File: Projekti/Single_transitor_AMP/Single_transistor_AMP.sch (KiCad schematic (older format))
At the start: 10 parts, among them P1 CONN_01X02, P2 CONN_01X02, Q1 BC549

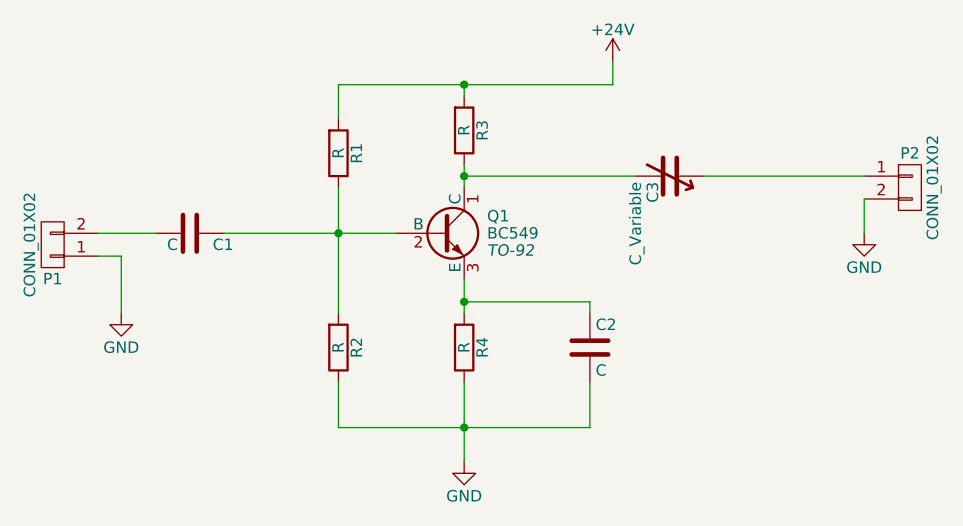
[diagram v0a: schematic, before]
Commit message: Single transitor amp
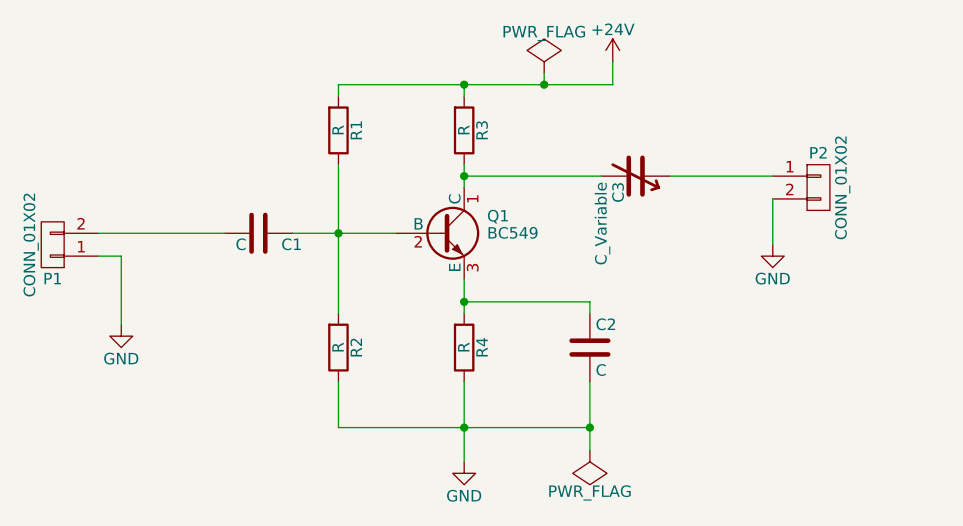
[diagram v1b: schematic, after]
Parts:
- Q1: footprint TO-92 -> TO_SOT_Packages_THT:TO-92_Inline_Wide
- R1, R2, R3, R4: footprint (none) -> Resistors_THT:R_Axial_DIN0309_L9.0mm_D3.2mm_P15.24mm_Horizontal
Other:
- moved on the sheet: C1, C3, P2, R1
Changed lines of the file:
@@
 encoding utf-8
 Sheet 1 1
-Title ""
-Date ""
-Rev ""
-Comp ""
+Title "Single transitor (BC549) amplifier"
+Date "2017-03-23"
+Rev "1.0"
+Comp "VeA"
 Comment1 ""
 Comment2 ""
@@
 F 0 "Q1" H 5800 4025 50  0000 L CNN
 F 1 "BC549" H 5800 3950 50  0000 L CNN
-F 2 "TO-92" H 5800 3875 50  0000 L CIN
-F 3 "" H 5600 3950 50  0000 L CNN
+F 2 "TO_SOT_Packages_THT:TO-92_Inline_Wide" H 5800 3875 50  0001 L CIN
+F 3 "http://pdf1.alldatasheet.com/datasheet-pdf/view/273461/DCCOM/BC549.html" H 5600 3950 50  0001 L CNN
 	1    5600 3950
 	1    0    0    -1
@@
 L R R1
 U 1 1 58D39335
-P 5150 3600
-F 0 "R1" V 5230 3600 50  0000 C CNN
-F 1 "R" V 5150 3600 50  0000 C CNN
-F 2 "" V 5080 3600 50  0000 C CNN
-F 3 "" H 5150 3600 50  0000 C CNN
-	1    5150 3600
+P 5150 3500
+F 0 "R1" V 5230 3500 50  0000 C CNN
+F 1 "R" V 5150 3500 50  0000 C CNN
+F 2 "Resistors_THT:R_Axial_DIN0309_L9.0mm_D3.2mm_P15.24mm_Horizontal" V 5080 3500 50  0001 C CNN
+F 3 "" H 5150 3500 50  0000 C CNN
+	1    5150 3500
 	1    0    0    1
 $EndComp
@@
 F 0 "R2" V 5230 4450 50  0000 C CNN
 F 1 "R" V 5150 4450 50  0000 C CNN
-F 2 "" V 5080 4450 50  0000 C CNN
+F 2 "Resistors_THT:R_Axial_DIN0309_L9.0mm_D3.2mm_P15.24mm_Horizontal" V 5080 4450 50  0001 C CNN
 F 3 "" H 5150 4450 50  0000 C CNN
 	1    5150 4450
@@
 $EndComp
 Wire Wire Line
-	4650 3950 5400 3950
-Wire Wire Line
-	5150 3750 5150 4300
+	4950 3950 5150 3950
+Wire Wire Line
+	5150 3950 5400 3950
+Wire Wire Line
+	5150 3650 5150 3950
+Wire Wire Line
+	5150 3950 5150 4300
 Connection ~ 5150 3950
 $Comp
@@
 F 0 "R4" V 5780 4450 50  0000 C CNN
 F 1 "R" V 5700 4450 50  0000 C CNN
-F 2 "" V 5630 4450 50  0000 C CNN
+F 2 "Resistors_THT:R_Axial_DIN0309_L9.0mm_D3.2mm_P15.24mm_Horizontal" V 5630 4450 50  0001 C CNN
 F 3 "" H 5700 4450 50  0000 C CNN
 	1    5700 4450
@@
 $EndComp
 Wire Wire Line
-	5700 4150 5700 4300
+	5700 4150 5700 4250
+Wire Wire Line
+	5700 4250 5700 4300
 Wire Wire Line
 	5150 4600 5150 4800
 Wire Wire Line
-	5150 4800 6250 4800
-Wire Wire Line
-	5700 4600 5700 4950
+	5150 4800 5700 4800
+Wire Wire Line
+	5700 4800 6250 4800
+Wire Wire Line
+	5700 4600 5700 4800
+Wire Wire Line
+	5700 4800 5700 4950
 $Comp
 L C C2
@@
 Connection ~ 5700 4250
 Wire Wire Line
-	6250 4800 6250 4600
+	6250 4600 6250 4800
+Wire Wire Line
+	6250 4800 6250 4900
 Connection ~ 5700 4800
 Wire Wire Line
-	5150 3300 6350 3300
-Wire Wire Line
-	5150 3300 5150 3450
+	5150 3300 5700 3300
+Wire Wire Line
+	5700 3300 6050 3300
+Wire Wire Line
+	6050 3300 6350 3300
+Wire Wire Line
+	5150 3300 5150 3350
 Connection ~ 5700 3300
 $Comp
 L C C1
 U 1 1 58D39704
-P 4500 3950
-F 0 "C1" V 4550 4050 50  0000 L CNN
-F 1 "C" V 4550 3850 50  0000 L CNN
-F 2 "" H 4538 3800 50  0000 C CNN
-F 3 "" H 4500 3950 50  0000 C CNN
-	1    4500 3950
+P 4800 3950
+F 0 "C1" V 4850 4050 50  0000 L CNN
+F 1 "C" V 4850 3850 50  0000 L CNN
+F 2 "" H 4838 3800 50  0000 C CNN
+F 3 "" H 4800 3950 50  0000 C CNN
+	1    4800 3950
 	0    1    1    0
 $EndComp
@@
 $EndComp
 Wire Wire Line
-	4100 3950 4350 3950
+	4100 3950 4650 3950
 Wire Wire Line
 	4100 4050 4200 4050
 Wire Wire Line
-	4200 4050 4200 4300
+	4200 4050 4200 4350
 $Comp
 L GND #PWR1
 U 1 1 58D39852
-P 4200 4300
-F 0 "#PWR1" H 4200 4050 50  0001 C CNN
-F 1 "GND" H 4200 4150 50  0000 C CNN
-F 2 "" H 4200 4300 50  0000 C CNN
-F 3 "" H 4200 4300 50  0000 C CNN
-	1    4200 4300
+P 4200 4350
+F 0 "#PWR1" H 4200 4100 50  0001 C CNN
+F 1 "GND" H 4200 4200 50  0000 C CNN
+F 2 "" H 4200 4350 50  0000 C CNN
+F 3 "" H 4200 4350 50  0000 C CNN
+	1    4200 4350
 	1    0    0    -1
 $EndComp
@@
 F 0 "R3" V 5780 3500 50  0000 C CNN
 F 1 "R" V 5700 3500 50  0000 C CNN
-F 2 "" V 5630 3500 50  0000 C CNN
+F 2 "Resistors_THT:R_Axial_DIN0309_L9.0mm_D3.2mm_P15.24mm_Horizontal" V 5630 3500 50  0001 C CNN
 F 3 "" H 5700 3500 50  0000 C CNN
 	1    5700 3500
@@
 	5700 3300 5700 3350
 Wire Wire Line
-	5700 3750 5700 3650
-Wire Wire Line
-	5700 3700 6450 3700
+	5700 3650 5700 3700
+Wire Wire Line
+	5700 3700 5700 3750
+Wire Wire Line
+	5700 3700 6300 3700
 Connection ~ 5700 3700
 $Comp
 L C_Variable C3
 U 1 1 58D3A0DB
-P 6600 3700
-F 0 "C3" H 6625 3625 50  0000 L CNN
-F 1 "C_Variable" H 6625 3550 50  0000 L CNN
-F 2 "" H 6600 3700 50  0000 C CNN
-F 3 "" H 6600 3700 50  0000 C CNN
-	1    6600 3700
+P 6450 3700
+F 0 "C3" H 6475 3625 50  0000 L CNN
+F 1 "C_Variable" H 6475 3550 50  0000 L CNN
+F 2 "" H 6450 3700 50  0000 C CNN
+F 3 "" H 6450 3700 50  0000 C CNN
+	1    6450 3700
 	0    1    1    0
 $EndComp
 Wire Wire Line
-	6750 3700 7450 3700
+	6600 3700 7050 3700
 $Comp
 L CONN_01X02 P2
 U 1 1 58D3A302
-P 7650 3750
-F 0 "P2" H 7650 3900 50  0000 C CNN
-F 1 "CONN_01X02" V 7750 3750 50  0000 C CNN
-F 2 "" H 7650 3750 50  0000 C CNN
-F 3 "" H 7650 3750 50  0000 C CNN
-	1    7650 3750
+P 7250 3750
+F 0 "P2" H 7250 3900 50  0000 C CNN
+F 1 "CONN_01X02" V 7350 3750 50  0000 C CNN
+F 2 "" H 7250 3750 50  0000 C CNN
+F 3 "" H 7250 3750 50  0000 C CNN
+	1    7250 3750
 	1    0    0    -1
 $EndComp
@@
 L GND #PWR4
 U 1 1 58D3A50E
-P 7450 3950
-F 0 "#PWR4" H 7450 3700 50  0001 C CNN
-F 1 "GND" H 7450 3800 50  0000 C CNN
-F 2 "" H 7450 3950 50  0000 C CNN
-F 3 "" H 7450 3950 50  0000 C CNN
-	1    7450 3950
-	1    0    0    -1
-$EndComp
-Wire Wire Line
-	7450 3800 7450 3950
+P 7050 4000
+F 0 "#PWR4" H 7050 3750 50  0001 C CNN
+F 1 "GND" H 7050 3850 50  0000 C CNN
+F 2 "" H 7050 4000 50  0000 C CNN
+F 3 "" H 7050 4000 50  0000 C CNN
+	1    7050 4000
+	1    0    0    -1
+$EndComp
+Wire Wire Line
+	7050 3800 7050 4000
+$Comp
+L PWR_FLAG #FLG1
+U 1 1 58D3AC4E
+P 6050 3250
+F 0 "#FLG1" H 6050 3345 50  0001 C CNN
+F 1 "PWR_FLAG" H 6050 3430 50  0000 C CNN
+F 2 "" H 6050 3250 50  0000 C CNN
+F 3 "" H 6050 3250 50  0000 C CNN
+	1    6050 3250
+	1    0    0    -1
+$EndComp
+Wire Wire Line
+	6050 3250 6050 3300
+Connection ~ 6050 3300
+$Comp
+L PWR_FLAG #FLG2
+U 1 1 58D3ADF0
+P 6250 4900
+F 0 "#FLG2" H 6250 4995 50  0001 C CNN
+F 1 "PWR_FLAG" H 6250 5080 50  0000 C CNN
+F 2 "" H 6250 4900 50  0000 C CNN
+F 3 "" H 6250 4900 50  0000 C CNN
+	1    6250 4900
+	-1   0    0    1
+$EndComp
+Connection ~ 6250 4800
 $EndSCHEMATC
